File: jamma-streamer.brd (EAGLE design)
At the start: 180.3 x 92 mm, 23 parts, among them IC1 LM7805, J1 Audio line out, J3 SDCARD, U2 ATMEGA328PB-AUR, U3 74HC4050D, U4 LP298X

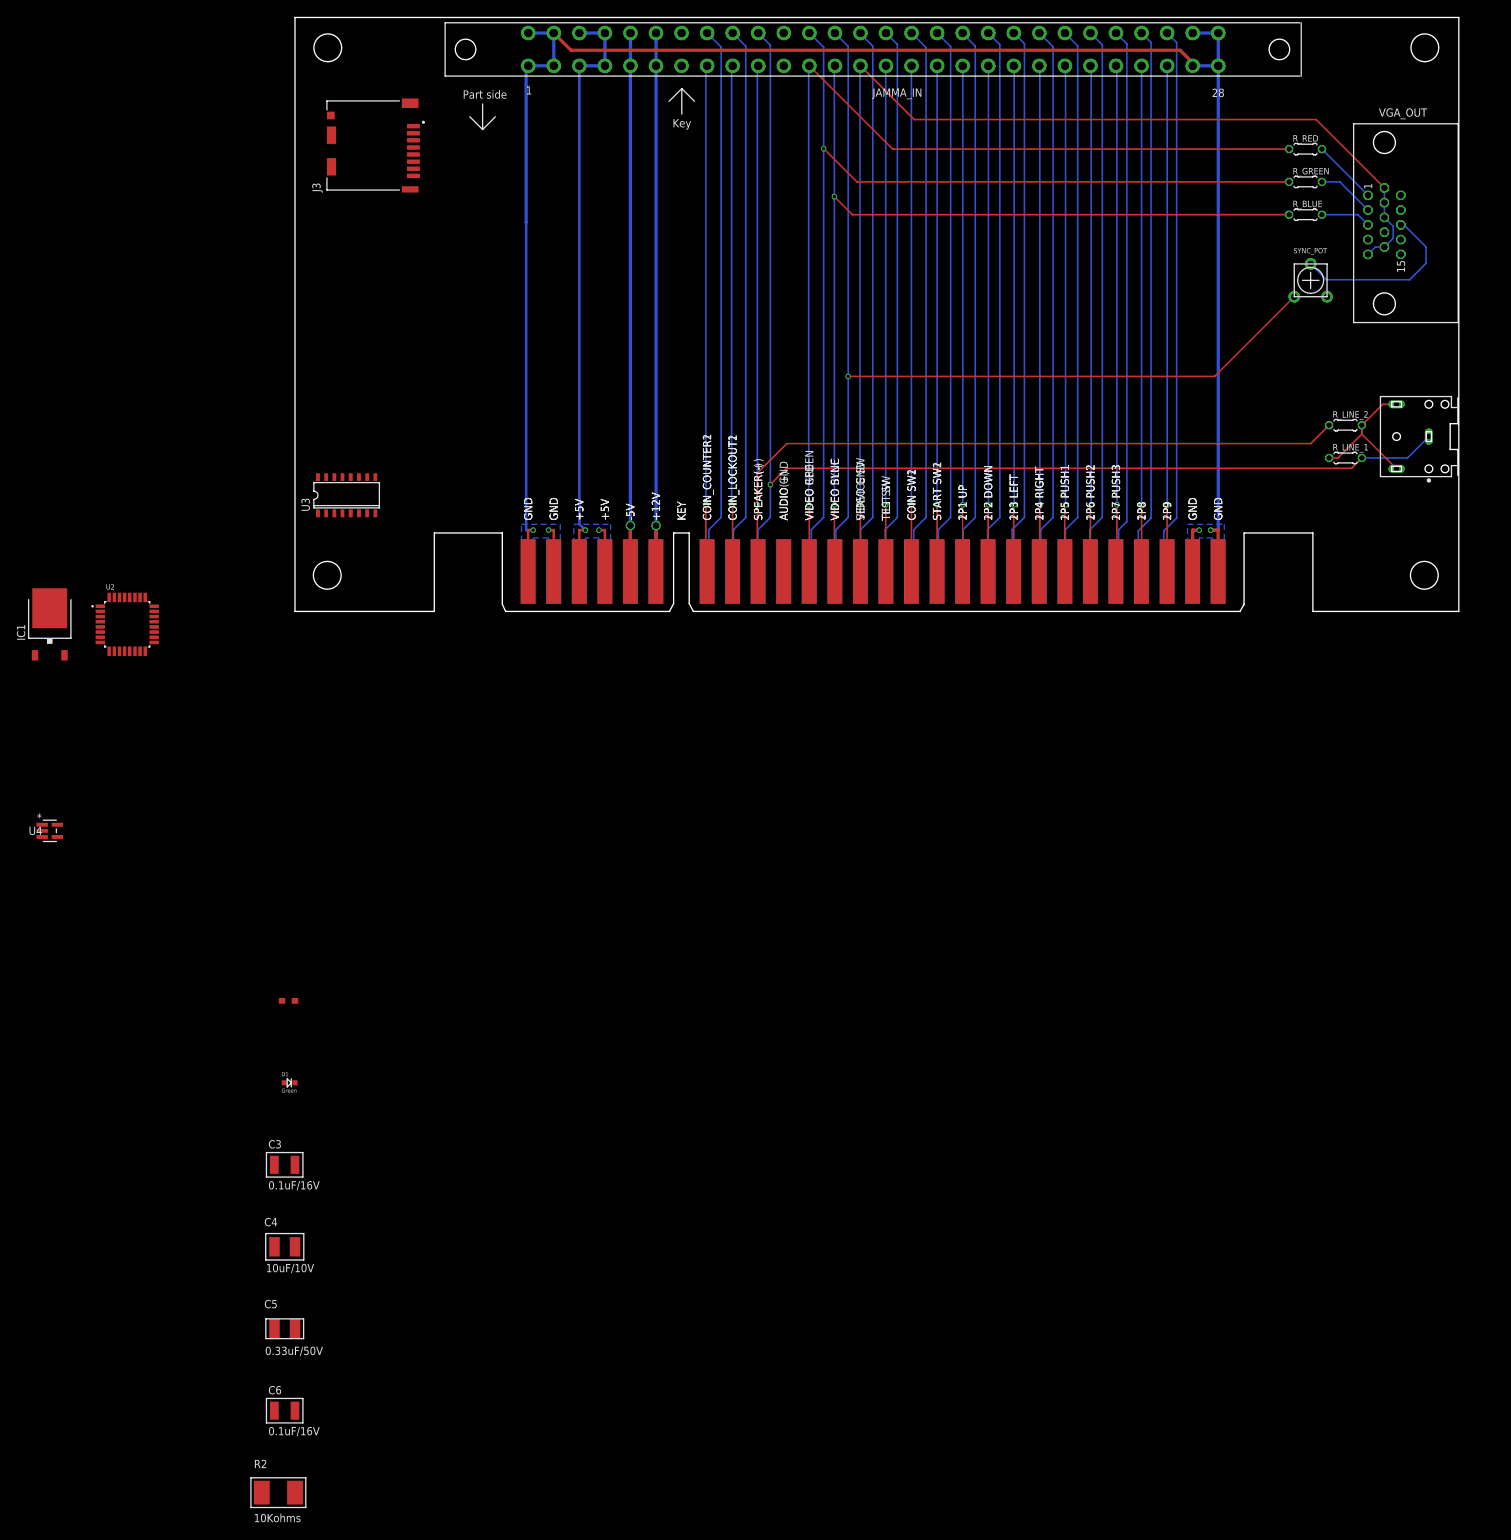
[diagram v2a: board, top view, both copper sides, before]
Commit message: Schematic with atmega328p wired
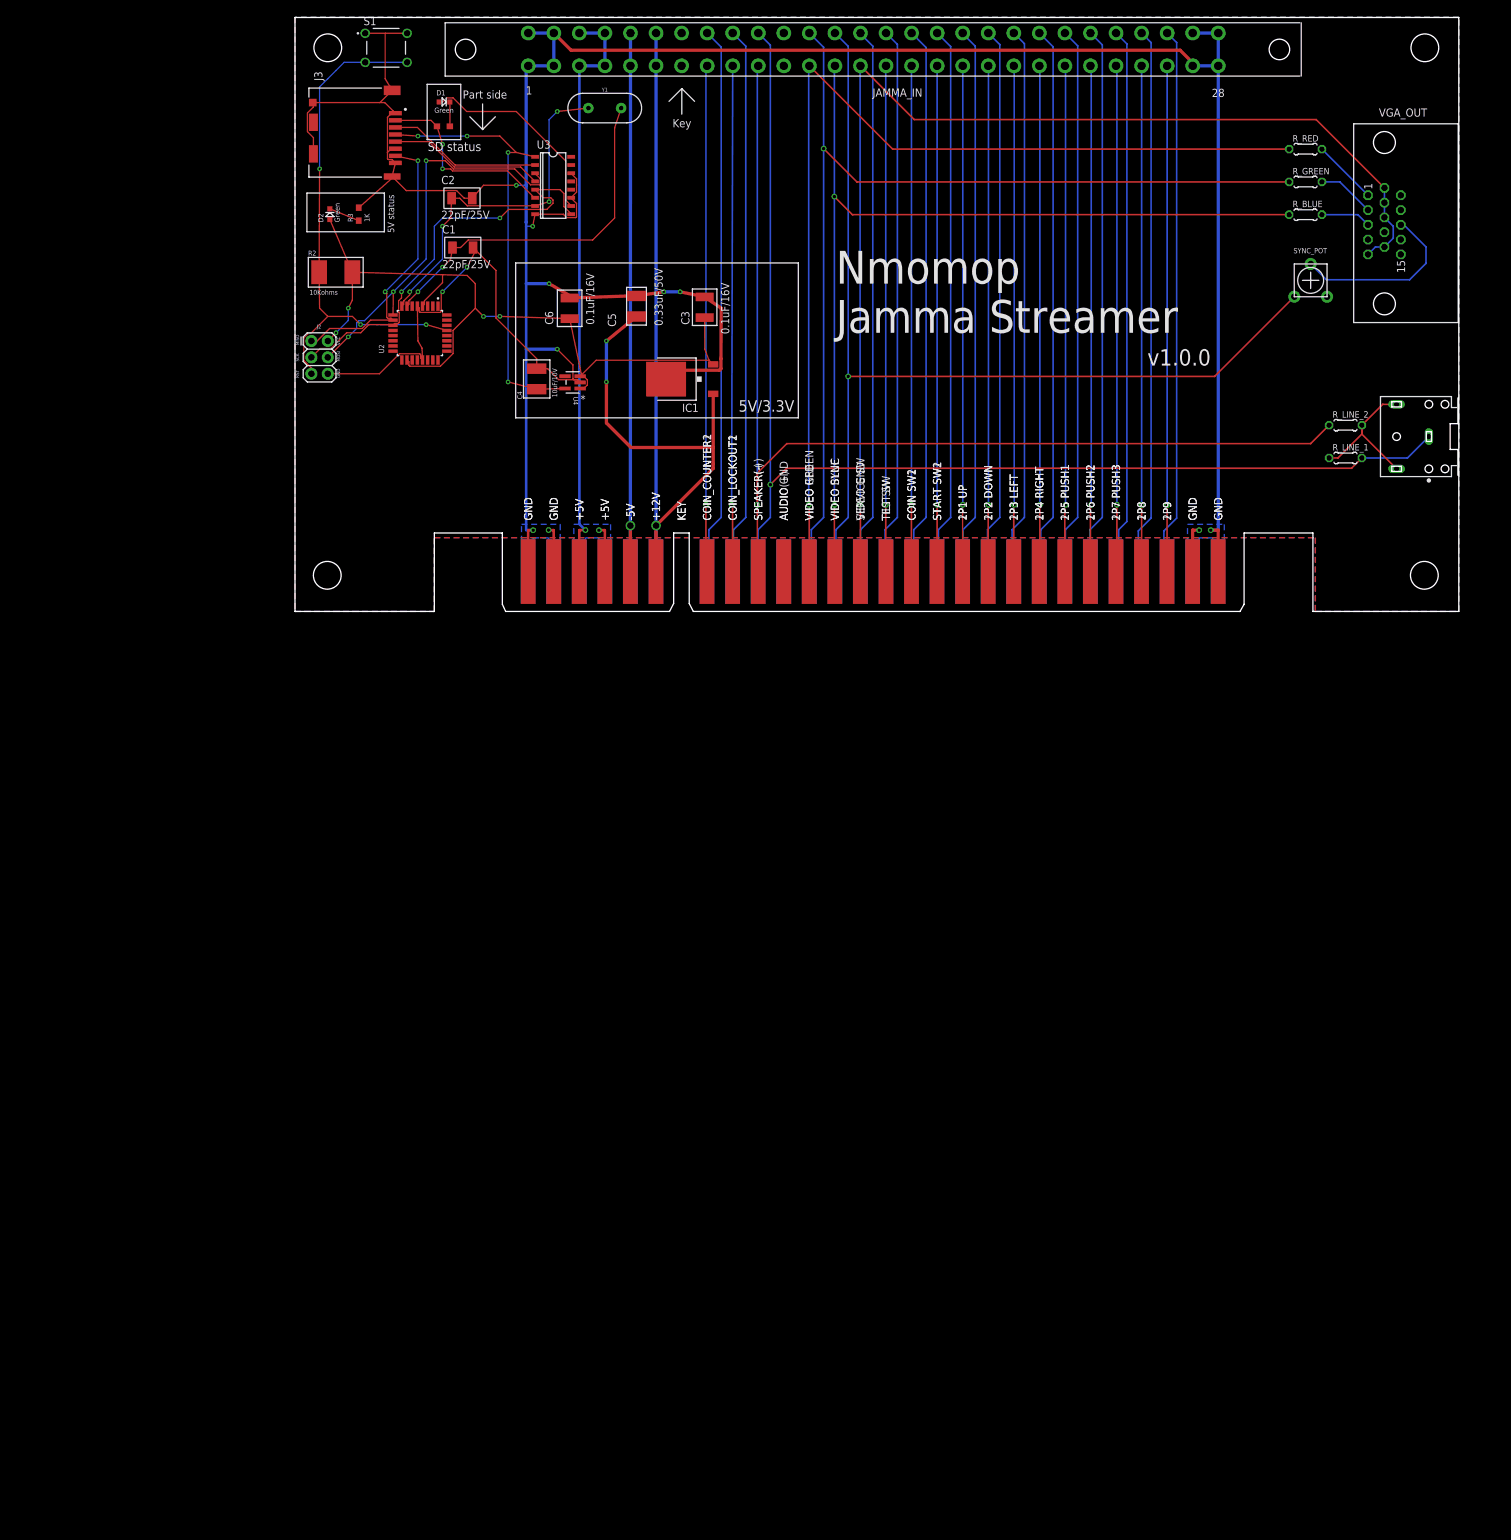
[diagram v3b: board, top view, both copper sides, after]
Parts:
- added C1, C2: 22pF/25V, CMS:KEMET-C1206C334M5RAC
- added D2: Green, CMS:604-APTD1608LCGCK
- added J2: ICSP, SparkFun-Connectors:2X3
- added R3: 1K, CMS:652-CHP0603FX1001ELF
- added S1: RESET SW, 1825910-7:SW_1825910-7
- added Y1: 16MHz, SparkFun-Clocks:HC49US
- moved R2 189.3 mm to (6.31, 52.6), turned to 180 degrees
- moved C6 176.4 mm to (42.6, 47.0), turned to 90 degrees
- moved C5 167.6 mm to (52.9, 47.3), turned to 90 degrees
- moved D1 153.9 mm to (23.2, 79.0)
- moved C3 148.0 mm to (63.5, 47.1), turned to 270 degrees
- moved C4 140.0 mm to (37.5, 36.0), turned to 270 degrees
- moved R1 137.6 mm to (23.0, 75.2), turned to 180 degrees
- moved U4 106.7 mm to (43.0, 35.5), turned to 180 degrees
- moved IC1 105.1 mm to (60.0, 36.0), turned to 90 degrees
- moved U2 64.0 mm to (19.4, 43.1), turned to 270 degrees
- moved U3 57.7 mm to (40.0, 66.0), turned to 270 degrees
- moved J3 3.44 mm to (9.21, 74.0)
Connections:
- removed net AVCC: U2.18
- removed net N$9: R2.2, U2.29
- new net N$12: D2.-, R3.1
- new net N$13: C1.1, U2.7, Y1.2
- new net RESET: J2.5, R2.2, S1.3, S1.4, U2.29
- net CLK: now also J2.3, U2.11
- net CS: now also C2.1, U2.8, Y1.1
- net DI: now also J2.4, U2.9
- net DO: now also J2.1, U2.10
- net GND: now also C1.2, C2.2, J2.6, R3.2, S1.1, S1.2; no longer U3.12, U3.15
- net VCC: now also D2.+, J2.2, U2.18
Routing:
- net GND: track 303.1 -> 555.0 mm, vias 4 -> 12
- net VCC: track 0.00 -> 124.1 mm, vias 0 -> 4
- net RESET: track 0.00 -> 81.5 mm, vias 0 -> 3
- net VCC_2: track 0.00 -> 68.6 mm, vias 0 -> 4
- net CLK: track 0.00 -> 65.4 mm, vias 0 -> 2
- net DI: track 0.00 -> 62.3 mm, vias 0 -> 3
- net JAMMA+12V: track 90.6 -> 151.5 mm, vias 1 -> 3
- net N$13: track 0.00 -> 56.1 mm, vias 0 -> 2
- net CS: track 0.00 -> 54.9 mm, vias 0 -> 4
- net DO: track 0.00 -> 45.2 mm, vias 0 -> 2
- net N$18: track 0.00 -> 31.2 mm
- net N$14: track 0.00 -> 29.7 mm, vias 0 -> 2
- net N$17: track 0.00 -> 24.2 mm
- net N$15: track 0.00 -> 24.1 mm
- net N$12: track 0.00 -> 4.83 mm
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- added copper zone on layer 1, net GND
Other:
- board text added: "5V status"
- board text added: "5V/3.3V"
- board text added: "GND"
- board text added: "MISO"
- board text added: "MOSI"
- board text added: "Nmomop Jamma Streamer"
- board text added: "RST"
- board text added: "SCK"
- board text added: "SD status"
- board text added: "VCC"
- board text added: "v1.0.0"

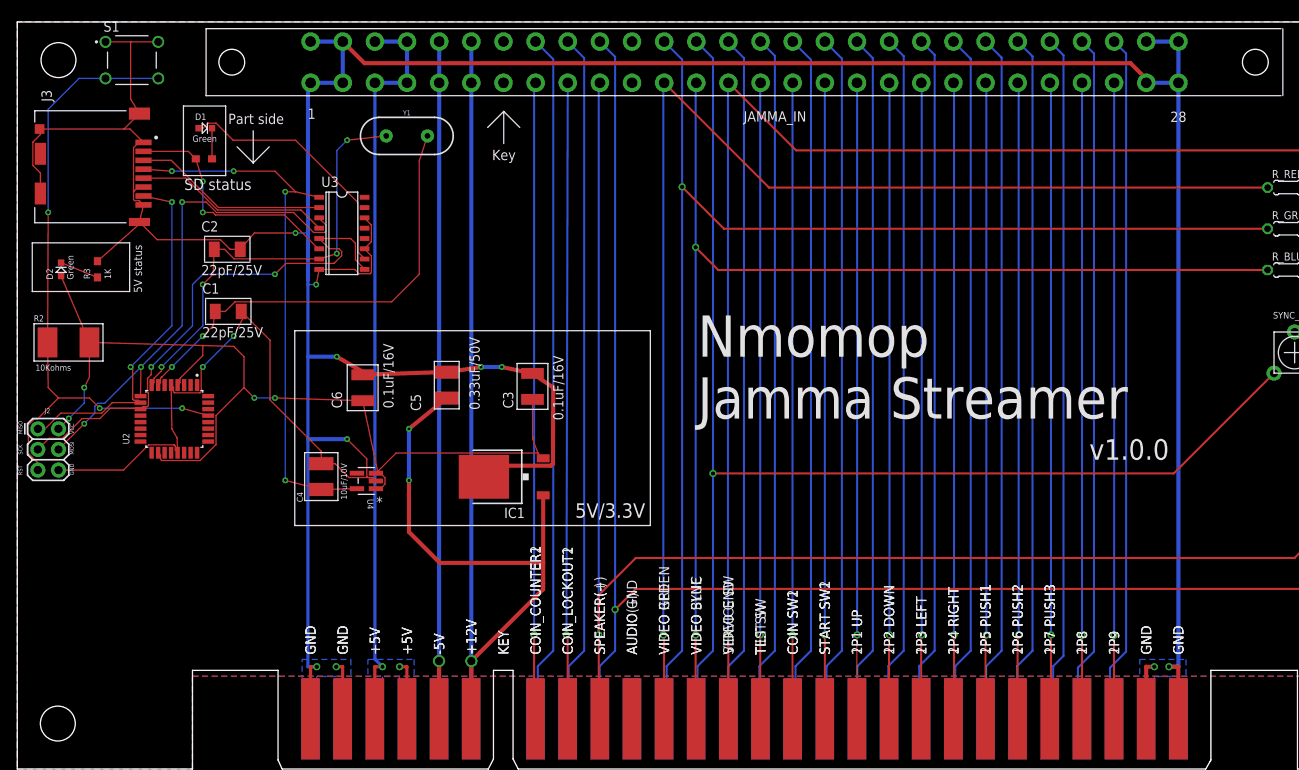
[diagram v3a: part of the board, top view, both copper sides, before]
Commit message: Adding button detection shift registers
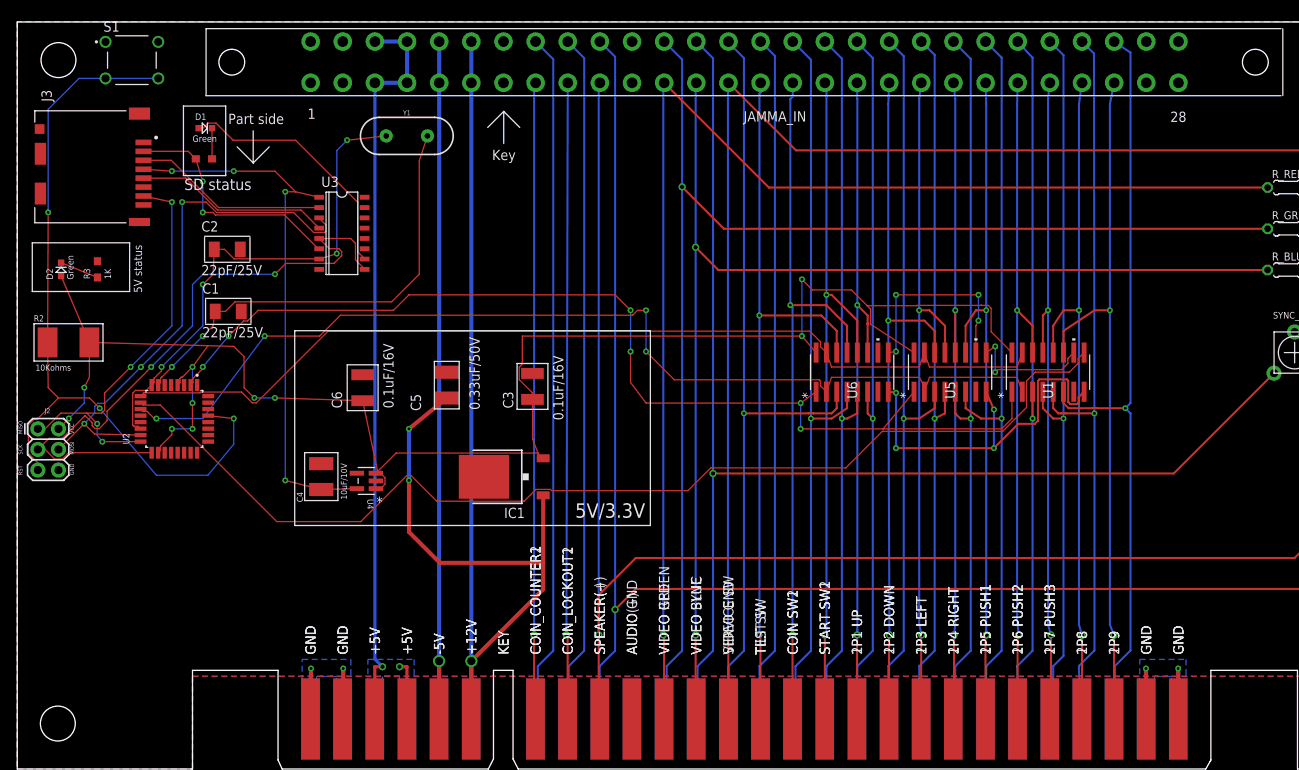
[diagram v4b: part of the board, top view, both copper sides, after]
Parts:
- added U1, U5, U6: CD74HC165MD16-M, CD74HC165M:D16-M
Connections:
- removed net A: JAMMA_IN._A, JAMMA_OUT_BTM._A
- removed net B: JAMMA_IN._B, JAMMA_OUT_BTM._B
- removed net N$5: JAMMA_IN._D, JAMMA_OUT_BTM._D
- removed net N$6: JAMMA_IN._C, JAMMA_OUT_BTM._C
- removed net N$7: JAMMA_IN.25, JAMMA_OUT_TOP.25
- removed net N$8: JAMMA_IN.26, JAMMA_OUT_TOP.26
- new net 25: JAMMA_IN.25, JAMMA_OUT_TOP.25, U1.12
- new net 26: JAMMA_IN.26, JAMMA_OUT_TOP.26, U1.11
- new net N$10: U1.10, U5.9
- new net N$9: U5.10, U6.9
- new net PD4: U1.1, U2.2, U5.1, U6.1
- new net PD5: U1.15, U2.9, U5.15, U6.15
- new net PD6: U1.9, U2.10
- new net PD7: U1.2, U2.11, U5.2, U6.2
- new net _A: JAMMA_IN._A, JAMMA_OUT_BTM._A, U1.3
- new net _B: JAMMA_IN._B, JAMMA_OUT_BTM._B, U1.4
- new net _C: JAMMA_IN._C, JAMMA_OUT_BTM._C, U1.5
- new net _D: JAMMA_IN._D, JAMMA_OUT_BTM._D, U1.6
- net 15: now also U6.14
- net 16: now also U6.13
- net 17: now also U6.12
- net 18: now also U6.11
- net 19: now also U5.14
- net 20: now also U5.13
- net 21: now also U5.12
- net 22: now also U5.11
- net 23: now also U1.14
- net 24: now also U1.13
- net CLK: now also U2.17; no longer U2.11
- net CS: now also U2.14
- net DI: now also U2.15; no longer U2.9
- net DO: now also U2.16; no longer U2.10
- net GND: now also U1.8, U5.8, U6.8
- net R: now also U6.3
- net T: now also U6.4
- net U: now also U6.5
- net V: now also U6.6
- net VCC: now also U1.16, U5.16, U6.16
- net W: now also U5.3
- net X: now also U5.4
- net Y: now also U5.5
- net Z: now also U5.6
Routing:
- net GND: track 555.0 -> 98.1 mm, vias 12 -> 8
- net PD6: track 0.00 -> 136.0 mm
- net PD4: track 0.00 -> 132.7 mm, vias 0 -> 6
- net PD7: track 0.00 -> 127.7 mm, vias 0 -> 4
- net PD5: track 0.00 -> 119.5 mm
- net _D: track 0.00 -> 95.1 mm, vias 0 -> 1
- net _C: track 0.00 -> 92.3 mm, vias 0 -> 1
- net _B: track 0.00 -> 90.4 mm, vias 0 -> 1
- net VCC: track 124.1 -> 213.9 mm, vias 4 -> 10
- net _A: track 0.00 -> 88.3 mm, vias 0 -> 1
- net 26: track 0.00 -> 87.7 mm, vias 0 -> 2
- net 25: track 0.00 -> 86.0 mm, vias 0 -> 2
- net B: track 85.3 -> 0.00 mm
- net N$5: track 85.1 -> 0.00 mm
- net N$6: track 85.1 -> 0.00 mm
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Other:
- board text removed: "Nmomop Jamma Streamer"
- board text removed: "v1.0.0"
